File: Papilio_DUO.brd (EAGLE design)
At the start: 101.6 x 55.9 mm, 122 parts, among them IC1 FT2232H, SW1 SWITCH-2CH-6P-3010010P1, SW2 EVQQ2, T100 MOSFET-NCHANNELSMD, U1 ARDUINO_MEGA_SHIELD, U100 PCA9306, U101 ATMEGA32U4-XUMU, U2 LTC3419EMS, U3 93C46B, X1 12MHz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

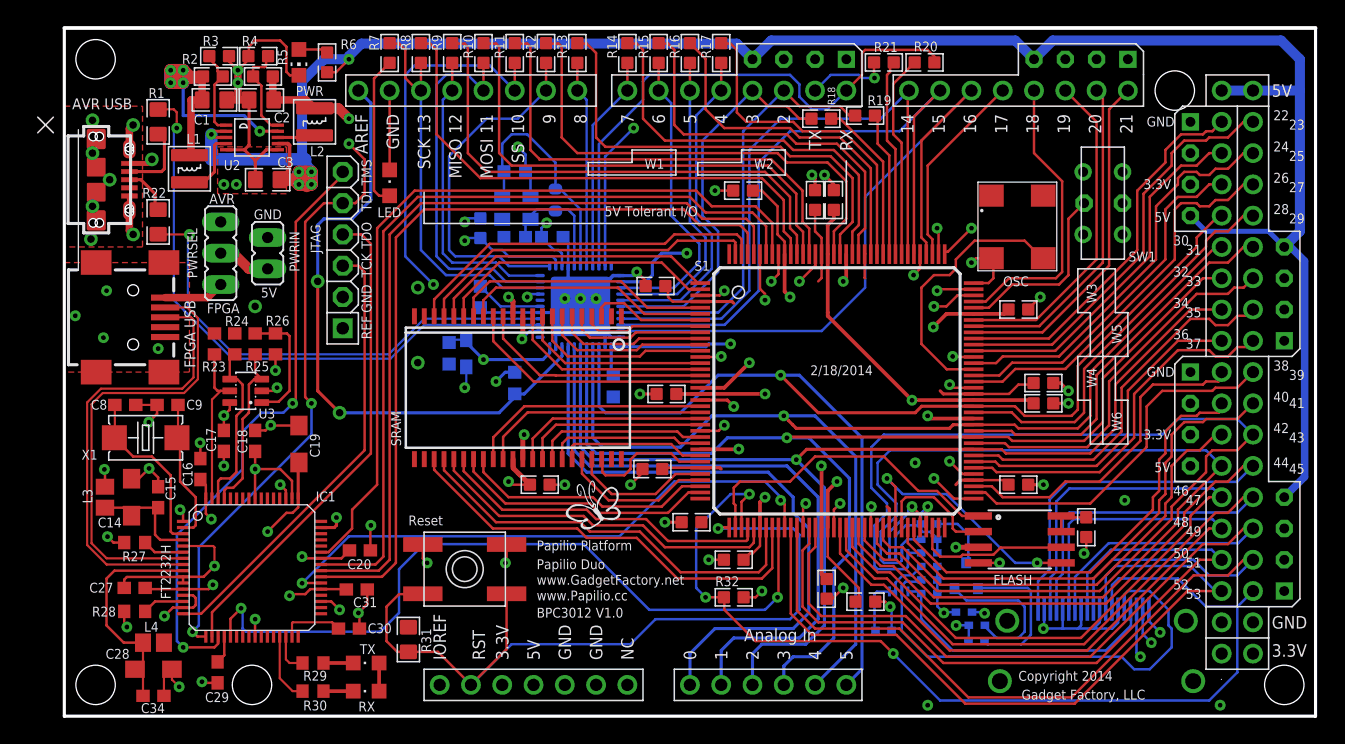
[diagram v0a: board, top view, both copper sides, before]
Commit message: Papilio DUO V1.0
Submitted for PCB
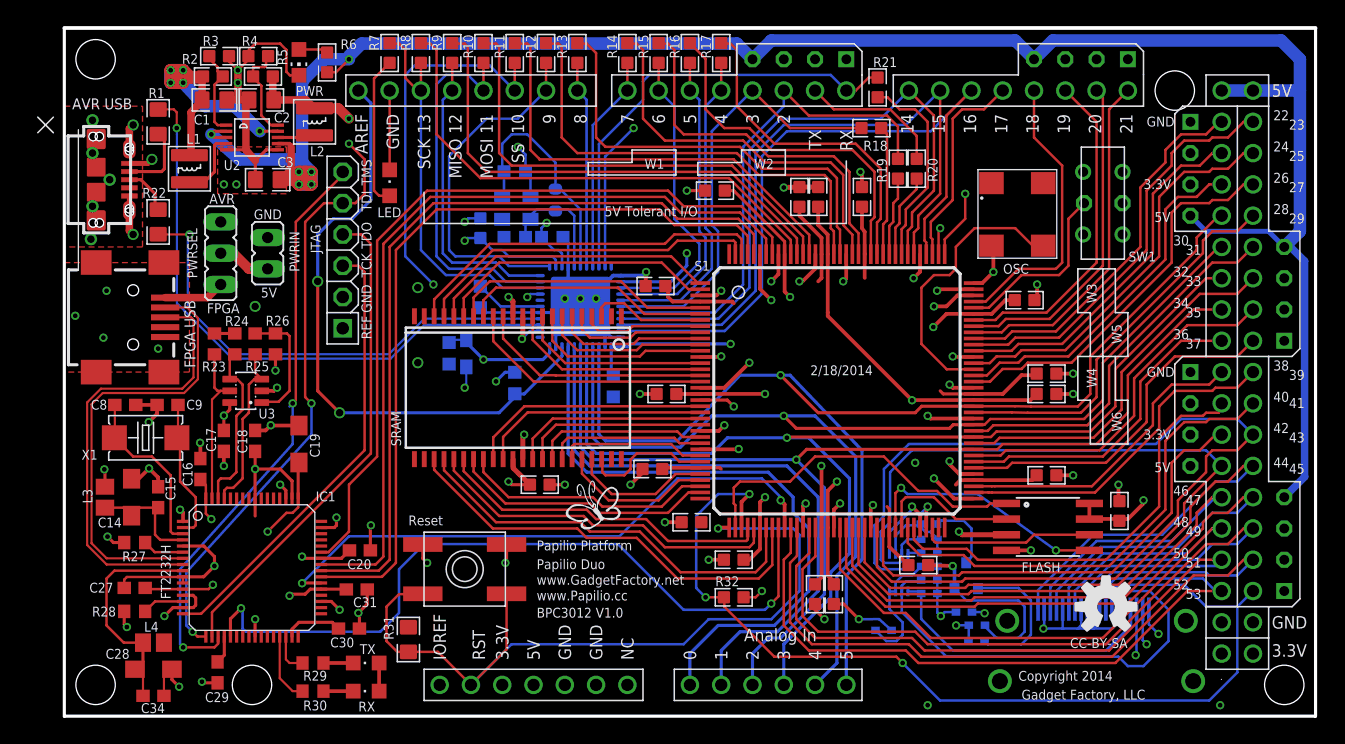
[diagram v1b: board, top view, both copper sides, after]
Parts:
- added C35, C36: .1uF, GadgetFactory:0603
- added U$9: (no value), SparkFun-Aesthetics:OSHW-LOGO-M
- moved R20 9.04 mm to (69.2, 44.5), turned to 90 degrees
- moved R19 5.08 mm to (67.7, 44.5), turned to 90 degrees
- moved R21 4.32 mm to (66.0, 51.1), turned to 90 degrees
- moved R18 4.13 mm to (65.5, 47.8)
- moved C26 3.00 mm to (85.7, 16.7), turned to 90 degrees
- moved C33 2.64 mm to (62.5, 9.91), turned to 270 degrees
- moved FLASH 2.50 mm to (79.9, 15.4)
- moved C25 2.41 mm to (79.8, 19.6)
- moved C5 2.29 mm to (52.8, 42.7)
- moved C6 1.30 mm to (59.7, 42.2)
- moved C7 1.30 mm to (61.2, 42.2)
- moved C32 1.03 mm to (61.0, 9.91)
- moved OSC 1.02 mm to (75.3, 43.3)
- moved C11 0.92 mm to (78.0, 33.8)
- moved C12 0.80 mm to (79.8, 27.8)
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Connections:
- net 3V3: now also C35.1, C36.1
- net GND: now also C35.2, C36.2
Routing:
- net ARD_RESET: track 71.5 -> 41.0 mm
- net 3V3: track 195.5 -> 213.5 mm
- net MEGA_D1: track 16.1 -> 6.85 mm
- net ATMEGA_D0/RX: track 45.9 -> 36.7 mm
- net GND: track 229.3 -> 237.0 mm, vias 76 -> 77
- net ATMEGA_D2: track 34.8 -> 41.1 mm
- net MEGA_D46: track 63.1 -> 57.0 mm
- net MEGA_D2: track 11.7 -> 6.43 mm
- net ATMEGA_D1/TX: track 34.9 -> 39.8 mm, vias 2 -> 1
- net MEGA_D47: track 66.7 -> 62.1 mm
- net MEGA_D48: track 60.3 -> 56.5 mm
- net ATMEGA_D3: track 31.7 -> 35.5 mm
- net MEGA_D45: track 67.5 -> 64.2 mm
- net 5V0: track 305.8 -> 302.8 mm
- net MEGA_D51: track 68.4 -> 65.6 mm
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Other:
- board text added: "CC-BY-SA"

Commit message: Papilio DUO V1.1
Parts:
- moved U$9 1.05 mm to (83.6, 8.64)
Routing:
- net 3V3: track 213.5 -> 216.7 mm
- net GND: track 237.0 -> 237.7 mm
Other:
- board text added: "BPC3012 V1.1"
- board text added: "CC-BY-SA 4.0"
- board text removed: "BPC3012 V1.0"
- board text removed: "CC-BY-SA"
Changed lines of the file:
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@@
 <setting verticaltext="up"/>
 </settings>
-<grid distance="0.05" unitdist="inch" unit="inch" style="lines" multiple="1" display="yes" altdistance="0.005" altunitdist="inch" altunit="inch"/>
+<grid distance="10" unitdist="mil" unit="mil" style="lines" multiple="1" display="yes" altdistance="1" altunitdist="mil" altunit="mil"/>
 <layers>
-<layer number="1" name="Top" color="4" fill="1" visible="yes" active="yes"/>
+<layer number="1" name="Top" color="4" fill="1" visible="no" active="yes"/>
 <layer number="2" name="Route2" color="6" fill="1" visible="no" active="yes"/>
 <layer number="3" name="Route3" color="11" fill="1" visible="no" active="yes"/>
 <layer number="14" name="Route14" color="1" fill="6" visible="no" active="no"/>
 <layer number="15" name="Route15" color="5" fill="1" visible="no" active="no"/>
-<layer number="16" name="Bottom" color="1" fill="1" visible="yes" active="yes"/>
+<layer number="16" name="Bottom" color="1" fill="1" visible="no" active="yes"/>
 <layer number="17" name="Pads" color="2" fill="1" visible="yes" active="yes"/>
 <layer number="18" name="Vias" color="2" fill="1" visible="yes" active="yes"/>
@@
 <layer number="22" name="bPlace" color="13" fill="1" visible="yes" active="yes"/>
 <layer number="23" name="tOrigins" color="15" fill="1" visible="yes" active="yes"/>
-<layer number="24" name="bOrigins" color="15" fill="1" visible="yes" active="yes"/>
+<layer number="24" name="bOrigins" color="15" fill="1" visible="no" active="yes"/>
 <layer number="25" name="tNames" color="7" fill="1" visible="yes" active="yes"/>
 <layer number="26" name="bNames" color="7" fill="1" visible="no" active="yes"/>
@@
 <layer number="29" name="tStop" color="12" fill="3" visible="no" active="yes"/>
 <layer number="30" name="bStop" color="12" fill="6" visible="no" active="yes"/>
-<layer number="31" name="tCream" color="7" fill="4" visible="no" active="yes"/>
+<layer number="31" name="tCream" color="7" fill="4" visible="yes" active="yes"/>
 <layer number="32" name="bCream" color="7" fill="5" visible="no" active="yes"/>
 <layer number="33" name="tFinish" color="6" fill="3" visible="no" active="yes"/>
@@
 <layer number="37" name="tTest" color="7" fill="1" visible="no" active="yes"/>
 <layer number="38" name="bTest" color="7" fill="1" visible="no" active="yes"/>
-<layer number="39" name="tKeepout" color="4" fill="11" visible="yes" active="yes"/>
-<layer number="40" name="bKeepout" color="1" fill="11" visible="yes" active="yes"/>
-<layer number="41" name="tRestrict" color="4" fill="10" visible="yes" active="yes"/>
-<layer number="42" name="bRestrict" color="1" fill="10" visible="yes" active="yes"/>
-<layer number="43" name="vRestrict" color="2" fill="10" visible="yes" active="yes"/>
+<layer number="39" name="tKeepout" color="4" fill="11" visible="no" active="yes"/>
+<layer number="40" name="bKeepout" color="1" fill="11" visible="no" active="yes"/>
+<layer number="41" name="tRestrict" color="4" fill="10" visible="no" active="yes"/>
+<layer number="42" name="bRestrict" color="1" fill="10" visible="no" active="yes"/>
+<layer number="43" name="vRestrict" color="2" fill="10" visible="no" active="yes"/>
 <layer number="44" name="Drills" color="7" fill="1" visible="no" active="yes"/>
 <layer number="45" name="Holes" color="7" fill="1" visible="yes" active="yes"/>
@@
 <text x="38.354" y="13.462" size="0.8" layer="130" font="vector" ratio="14">Papilio Platform</text>
 <text x="38.354" y="11.938" size="0.8" layer="130" font="vector" ratio="14">Papilio Duo</text>
-<text x="38.354" y="8.001" size="0.8" layer="130" font="vector" ratio="14">BPC3012 V1.0</text>
+<text x="38.354" y="8.001" size="0.8" layer="130" font="vector" ratio="14">BPC3012 V1.1</text>
 <text x="38.354" y="10.668" size="0.8" layer="130" font="vector" ratio="14">www.GadgetFactory.net</text>
 <text x="77.47" y="2.8702" size="0.8" layer="130" font="vector" ratio="14">Copyright 2014</text>
@@
 <text x="7.62" y="-19.05" size="2.54" layer="51" font="vector" ratio="14">Top silkscreen is on layer 130: tSilk</text>
 <text x="7.62" y="-22.86" size="2.54" layer="51" font="vector" ratio="14">Bottom silkscreen is on layer 200</text>
-<text x="81.661" y="5.5372" size="0.8" layer="130" font="vector" ratio="14">CC-BY-SA</text>
+<text x="77.851" y="5.0292" size="0.8" layer="130" font="vector" ratio="14">CC-BY-SA 4.0</text>
 </plain>
 <attributes>
@@
 <attribute name="VALUE" x="70.742" y="11.7182" size="0.05" layer="27" font="vector" ratio="0" rot="R180"/>
 </element>
-<element name="U$9" library="SparkFun-Aesthetics" package="OSHW-LOGO-M" value="" x="84.582" y="8.89"/>
+<element name="U$9" library="SparkFun-Aesthetics" package="OSHW-LOGO-M" value="" x="83.566" y="8.636"/>
 </elements>
 <signals>
@@
 <wire x1="15.49" y1="7.87" x2="15.494" y2="7.874" width="0.2032" layer="1"/>
 <via x="15.494" y="7.874" extent="1-16" drill="0.381"/>
-<wire x1="9.64" y1="11.315" x2="9.64" y2="10.815" width="0.2032" layer="1"/>
 <wire x1="9.64" y1="9.815" x2="10.45" y2="9.815" width="0.254" layer="1"/>
 <wire x1="9.64" y1="8.815" x2="10.466" y2="8.815" width="0.254" layer="1"/>
@@
 <wire x1="8.815" y1="8.815" x2="8.128" y2="8.128" width="0.254" layer="1"/>
 <via x="8.128" y="8.128" extent="1-16" drill="0.381"/>
-<wire x1="9.64" y1="11.315" x2="11.315" y2="11.315" width="0.254" layer="1"/>
+<wire x1="9.64" y1="11.315" x2="10.414" y2="11.315" width="0.254" layer="1"/>
+<wire x1="10.414" y1="11.315" x2="11.315" y2="11.315" width="0.254" layer="1"/>
 <wire x1="11.315" y1="11.315" x2="12.192" y2="12.192" width="0.254" layer="1"/>
 <via x="12.192" y="12.192" extent="1-16" drill="0.381"/>
@@
 <wire x1="62.484" y1="9.106" x2="63.284" y2="9.106" width="0.254" layer="1"/>
 <wire x1="63.284" y1="9.106" x2="64.516" y2="7.874" width="0.254" layer="1"/>
+<wire x1="9.64" y1="10.815" x2="10.414" y2="10.815" width="0.2032" layer="1"/>
+<wire x1="10.414" y1="10.815" x2="10.414" y2="11.315" width="0.2032" layer="1"/>
+<wire x1="2.286" y1="45.72" x2="2.5908" y2="46.863" width="0" layer="19" extent="1-1"/>
+<wire x1="8.188" y1="30.785" x2="7.62" y2="29.845" width="0" layer="19" extent="1-1"/>
+<wire x1="2.5908" y1="44.577" x2="2.286" y2="45.72" width="0" layer="19" extent="1-1"/>
+<wire x1="2.5908" y1="42.545" x2="2.286" y2="41.402" width="0" layer="19" extent="1-1"/>
+<wire x1="2.5908" y1="40.259" x2="2.286" y2="41.402" width="0" layer="19" extent="1-1"/>
 </signal>
 <signal name="OSC_IN">
@@
 <wire x1="85.8138" y1="16.002" x2="85.6742" y2="15.8624" width="0.3048" layer="1"/>
 <wire x1="12.192" y1="31.076" x2="13.843" y2="31.076" width="0.254" layer="1"/>
+<wire x1="53.988" y1="37.516" x2="53.988" y2="35.954" width="0.254" layer="1"/>
+<wire x1="53.988" y1="35.954" x2="53.975" y2="35.941" width="0.254" layer="1"/>
+<wire x1="51.638" y1="17.666" x2="53.099" y2="17.666" width="0.254" layer="1"/>
+<wire x1="53.099" y1="17.666" x2="53.213" y2="17.78" width="0.254" layer="1"/>
 </signal>
 <signal name="1V2">

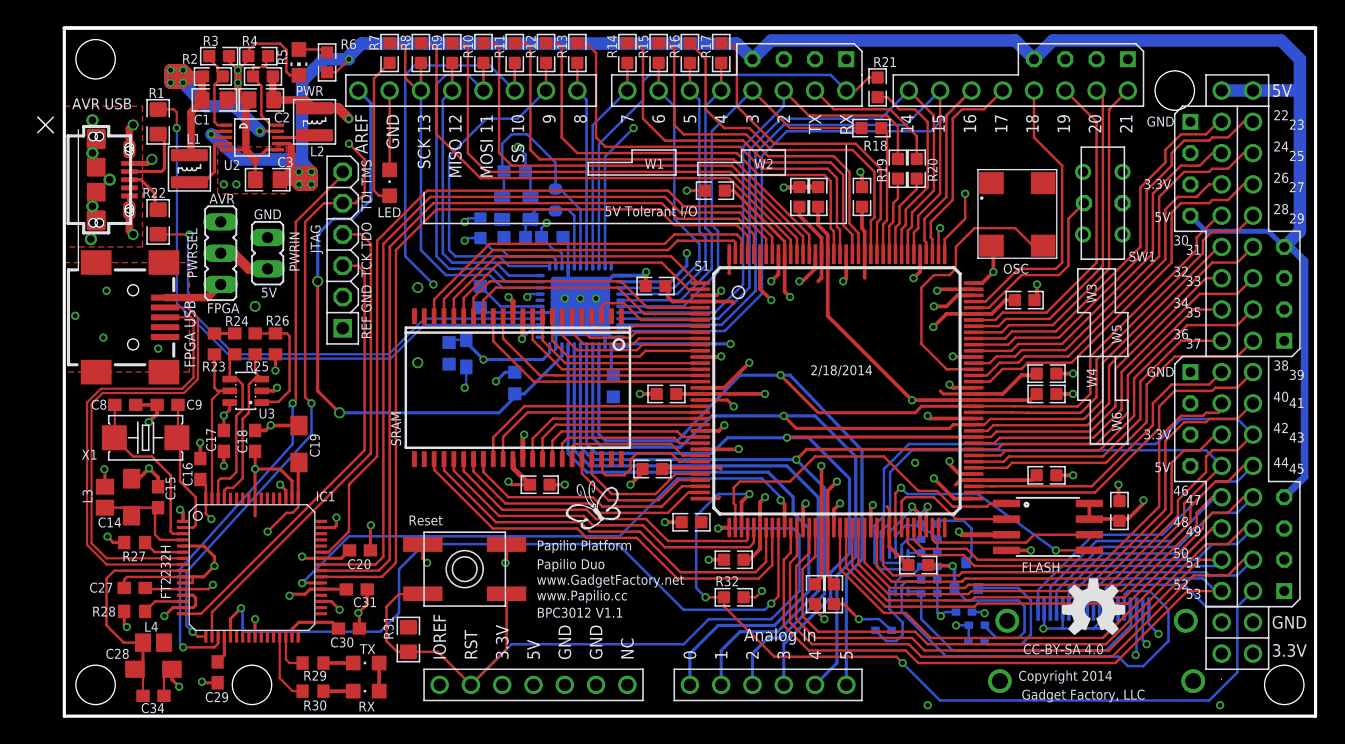
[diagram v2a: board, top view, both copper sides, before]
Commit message: Papilio DUO V1.2
Changed size to 100CM for cheaper manufacturing
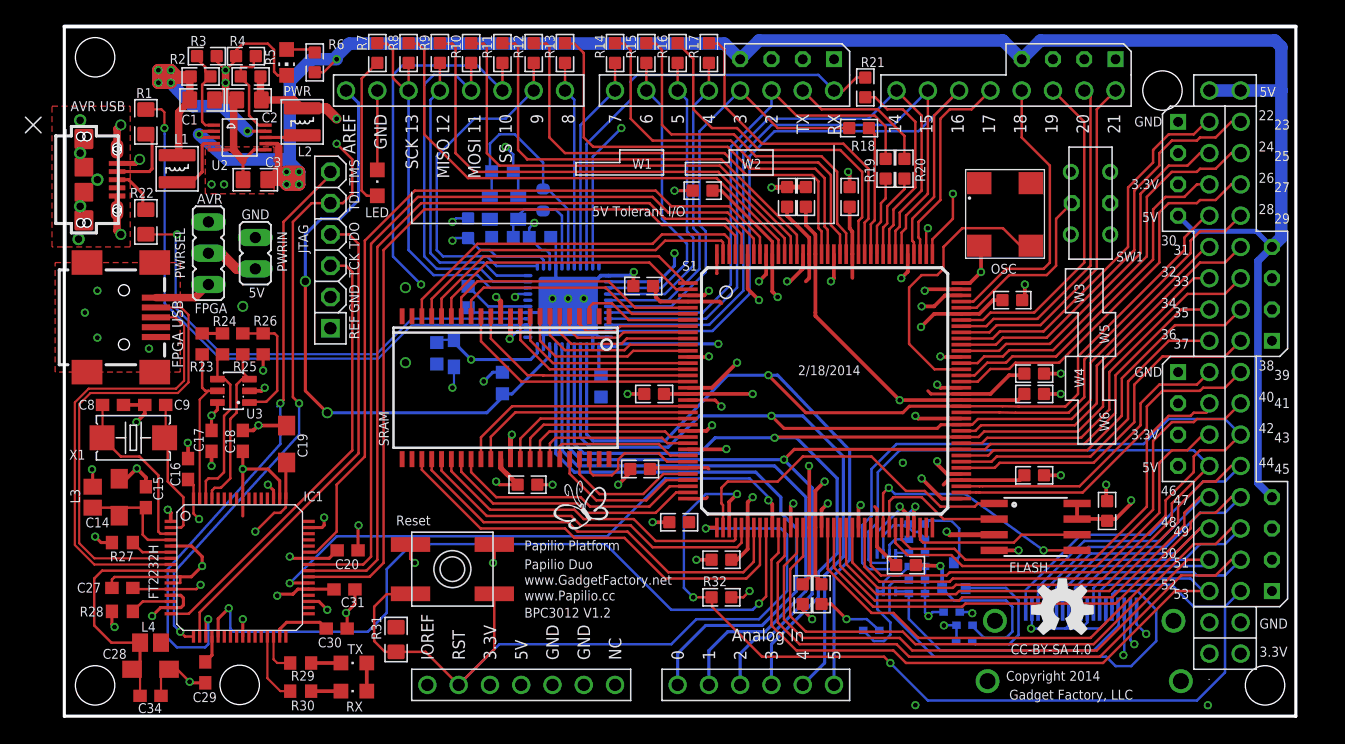
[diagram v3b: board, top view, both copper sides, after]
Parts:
- moved U$9 2.52 mm to (81.0, 8.64)
- moved L100 1.00 mm to (31.6, 29.5)
- moved C3 1.00 mm to (15.5, 43.6)
- moved PWRIN 1.00 mm to (15.5, 37.6)
- moved R5 1.00 mm to (15.1, 51.9)
- moved U1 1.00 mm to (7.89, 53.3)
- moved C8 1.00 mm to (3.95, 25.3)
- moved AVRUSB 1.00 mm to (1.59, 43.6)
- moved C1 1.00 mm to (11.2, 50.0)
- moved C10 1.00 mm to (47.9, 26.2)
- moved C100 1.00 mm to (65.5, 6.97)
- moved C101 1.00 mm to (43.6, 26.8)
- moved C102 1.00 mm to (35.6, 27.1)
- moved C103 1.00 mm to (32.8, 34.0)
- moved C104 1.00 mm to (30.2, 29.5)
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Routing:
- net AD3-JTAG_TMS: track 103.7 -> 106.5 mm
- net 5V0: track 302.8 -> 300.8 mm
- net N$49: track 18.7 -> 19.4 mm
- net FTUSB_N: track 36.7 -> 37.2 mm
- net GND: track 237.7 -> 238.2 mm, vias 77 -> 76
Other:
- board size 101.6 x 55.9 mm -> 100 x 56 mm
- board text added: "BPC3012 V1.2"
- board text removed: "BPC3012 V1.1"
